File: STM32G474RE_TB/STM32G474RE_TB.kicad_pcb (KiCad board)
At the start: 2 copper layers, 4 parts, among them U1 STM32G474RETx, Y1 ABM8G-24.000MHZ-18-D2Y-T

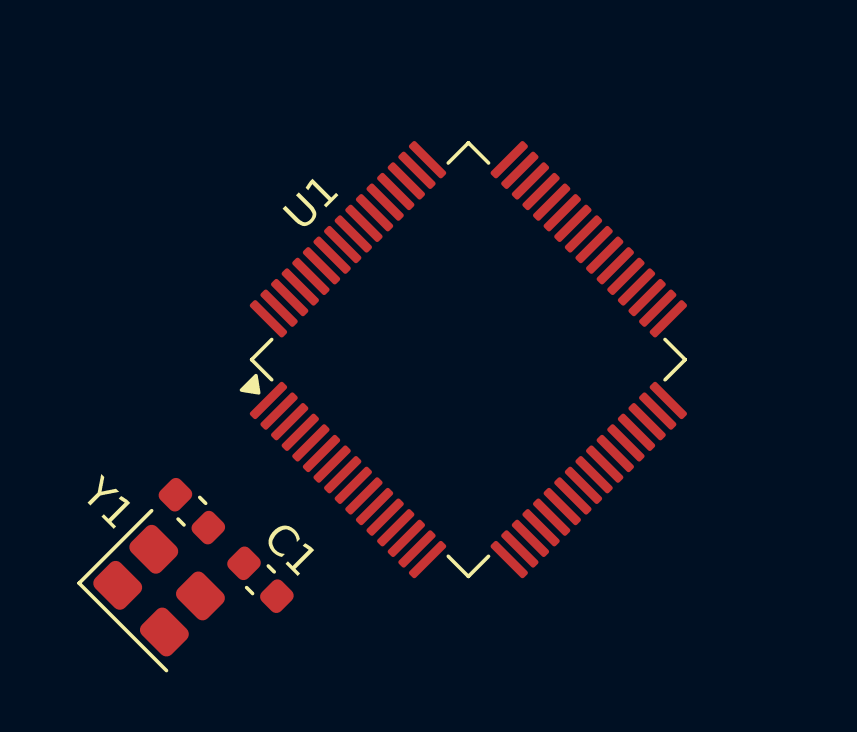
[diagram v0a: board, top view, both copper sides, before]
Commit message: Rotated STM32 and adjusted xosc capacitor values.
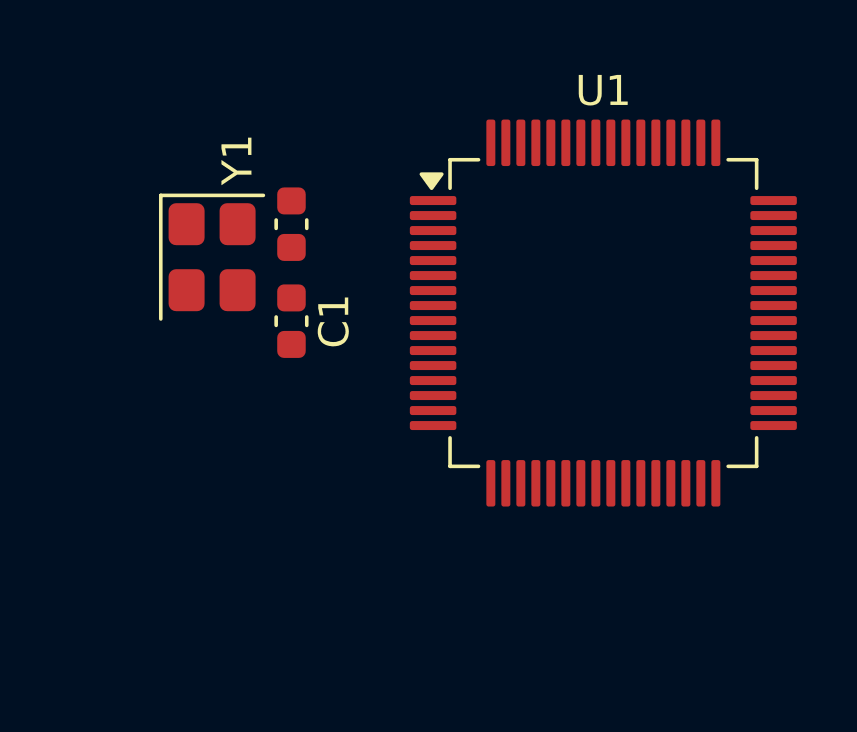
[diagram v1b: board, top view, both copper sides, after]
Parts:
- moved Y1 11.3 mm to (72.6, 35.7), turned to -90 degrees
- moved C2 10.1 mm to (75.2, 34.6), turned to 90 degrees
- moved C1 8.68 mm to (75.2, 37.9), turned to -90 degrees
- moved U1 4.76 mm to (85.6, 37.6), turned to 0 degrees

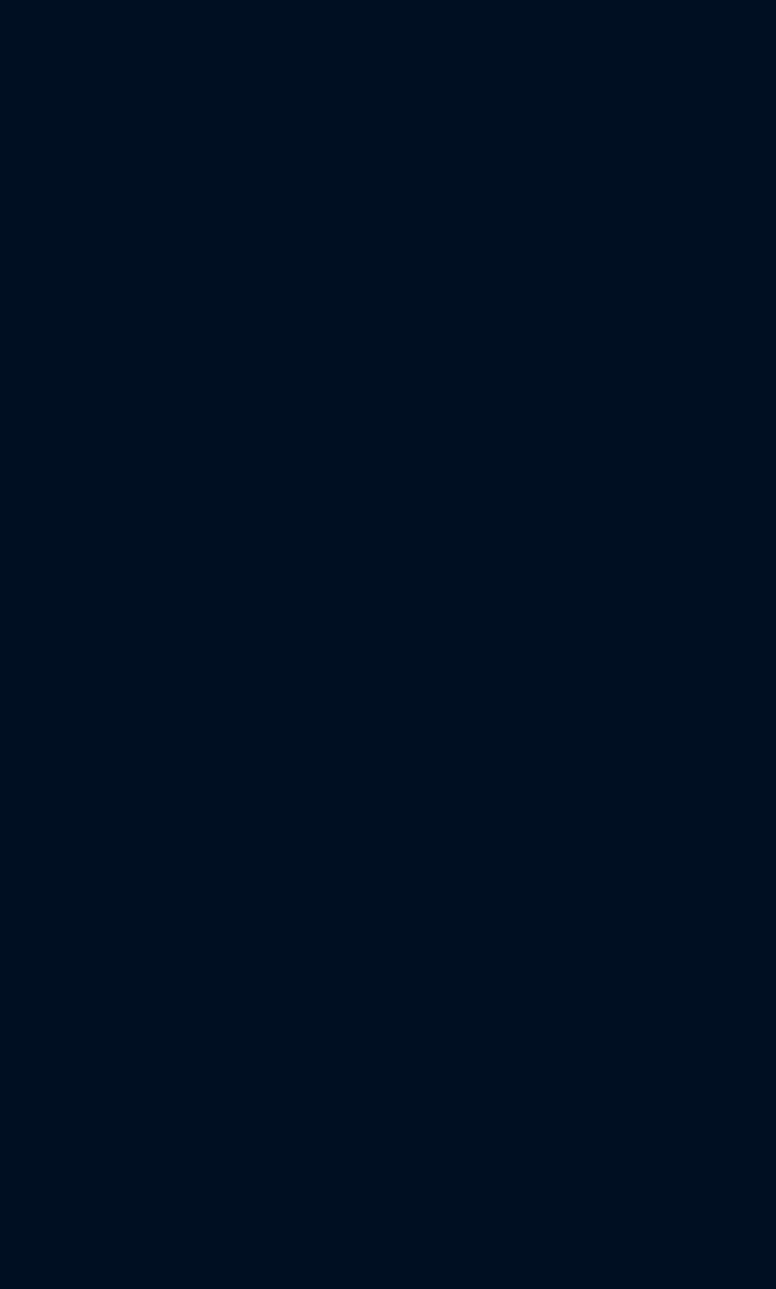
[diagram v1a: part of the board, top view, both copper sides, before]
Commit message: Added temporary STM32Cubeide project for pin config.
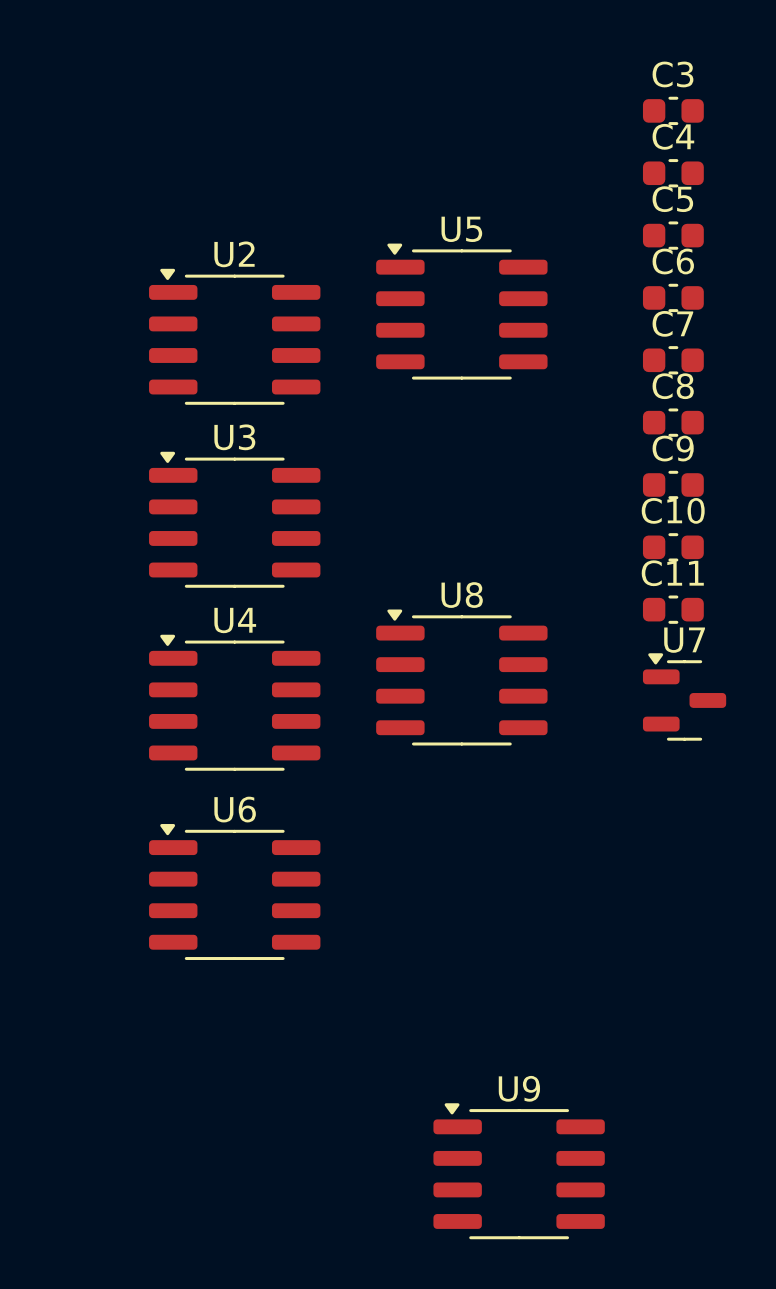
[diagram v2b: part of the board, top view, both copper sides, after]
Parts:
- added C10: 0.1uf, Capacitor_SMD:C_0603_1608Metric, F.Cu at (120.8, 39.9)
- added C11: 0.1uf, Capacitor_SMD:C_0603_1608Metric, F.Cu at (120.8, 42.4)
- added C3: 0.1uf, Capacitor_SMD:C_0603_1608Metric, F.Cu at (120.8, 22.3)
- added C4: 0.1uf, Capacitor_SMD:C_0603_1608Metric, F.Cu at (120.8, 24.8)
- added C5: 0.1uf, Capacitor_SMD:C_0603_1608Metric, F.Cu at (120.8, 27.3)
- added C6: 0.1uf, Capacitor_SMD:C_0603_1608Metric, F.Cu at (120.8, 29.8)
- added C7: 0.47uF, Capacitor_SMD:C_0603_1608Metric, F.Cu at (120.8, 32.3)
- added C8: 0.1uf, Capacitor_SMD:C_0603_1608Metric, F.Cu at (120.8, 34.8)
- added C9: 0.1uf, Capacitor_SMD:C_0603_1608Metric, F.Cu at (120.8, 37.3)
- added U2: MCP4921-ESN, Package_SO:SOIC-8_3.9x4.9mm_P1.27mm, F.Cu at (103.1, 31.5)
- added U3: MCP4921-ESN, Package_SO:SOIC-8_3.9x4.9mm_P1.27mm, F.Cu at (103.1, 38.9)
- added U4: MCP4921-ESN, Package_SO:SOIC-8_3.9x4.9mm_P1.27mm, F.Cu at (103.1, 46.2)
- added U5: OPA1678, Package_SO:SOIC-8_3.9x4.9mm_P1.27mm, F.Cu at (112.3, 30.5)
- added U6: MCP4921-ESN, Package_SO:SOIC-8_3.9x4.9mm_P1.27mm, F.Cu at (103.1, 53.8)
- added U7: REF3125, Package_TO_SOT_SMD:SOT-23, F.Cu at (121.2, 46.0)
- added U8: OPA1678, Package_SO:SOIC-8_3.9x4.9mm_P1.27mm, F.Cu at (112.3, 45.2)
- added U9: OPA1678, Package_SO:SOIC-8_3.9x4.9mm_P1.27mm, F.Cu at (114.6, 65.1)
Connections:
- U1 pad 35: unconnected-(U1-PB13-Pad35) -> /SPI1_SCK
- U1 pad 37: unconnected-(U1-PB15-Pad37) -> /SPI1_MOSI
- U1 pad 38: unconnected-(U1-PC6-Pad38) -> /DAC1_CS
- U1 pad 39: unconnected-(U1-PC7-Pad39) -> /DAC2_CS
- U1 pad 40: unconnected-(U1-PC8-Pad40) -> /DAC3_CS
- U1 pad 41: unconnected-(U1-PC9-Pad41) -> /DAC4_CS

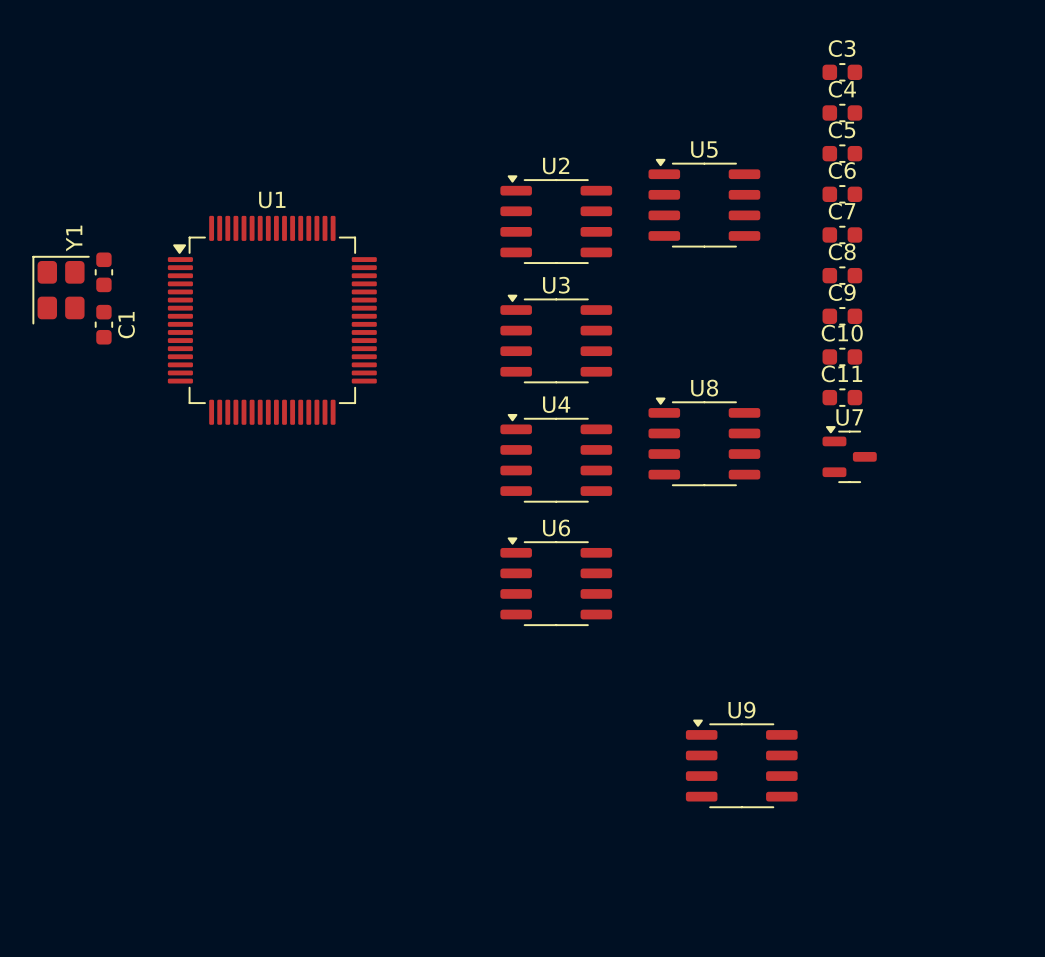
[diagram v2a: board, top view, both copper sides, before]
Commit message: Added power LDO and built DAC buffer circuits Added pin descriptions
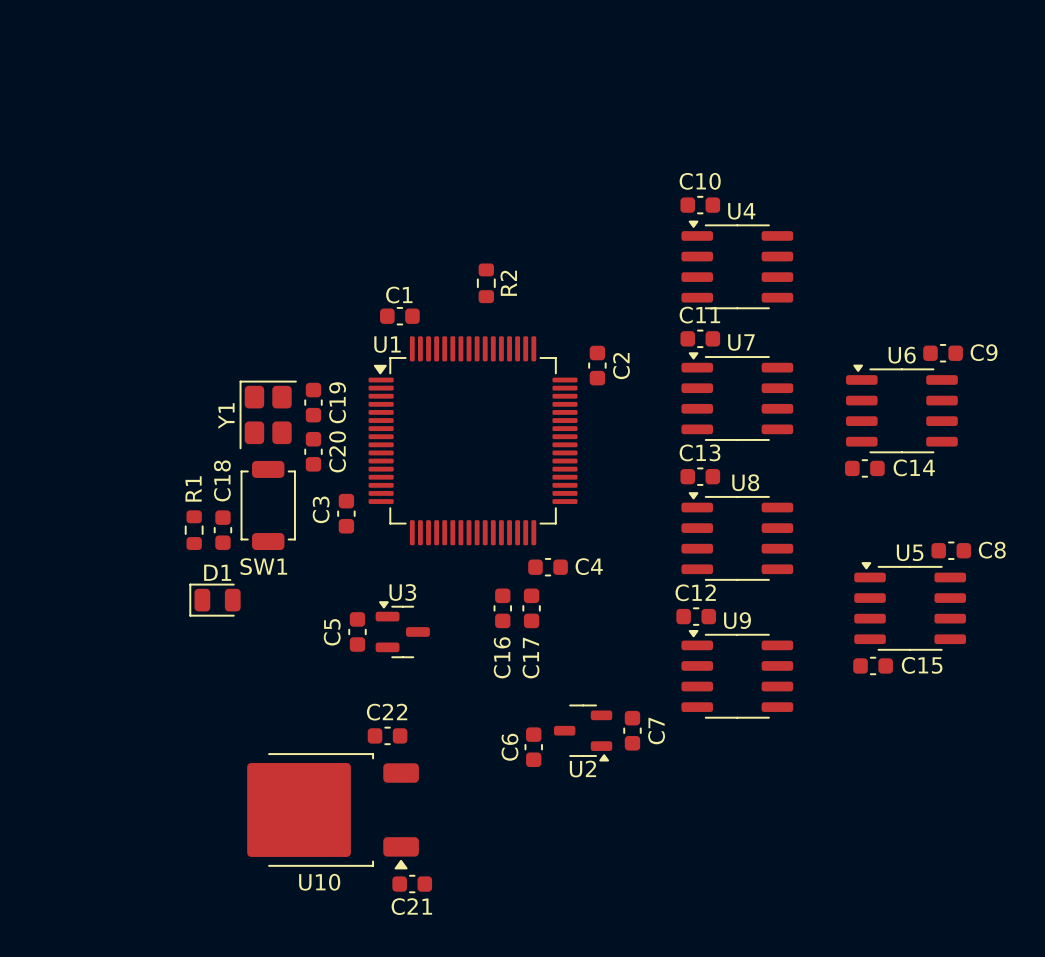
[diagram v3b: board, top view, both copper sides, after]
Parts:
- added C12: 0.1uf, Capacitor_SMD:C_0603_1608Metric, F.Cu at (111.8, 55.9)
- added C13: 0.1uf, Capacitor_SMD:C_0603_1608Metric, F.Cu at (112.0, 47.2)
- added C14: 0.1uf, Capacitor_SMD:C_0603_1608Metric, F.Cu at (122.2, 46.7)
- added C15: 0.1uf, Capacitor_SMD:C_0603_1608Metric, F.Cu at (122.7, 58.9)
- added C16: 0.1uf, Capacitor_SMD:C_0603_1608Metric, F.Cu at (99.8, 55.4)
- added C17: 1uf, Capacitor_SMD:C_0603_1608Metric, F.Cu at (101.6, 55.4)
- added C18: 0.1uf, Capacitor_SMD:C_0603_1608Metric, F.Cu at (82.5, 50.5)
- added C19: 22pf, Capacitor_SMD:C_0603_1608Metric, F.Cu at (88.1, 42.7)
- added C20: 22pf, Capacitor_SMD:C_0603_1608Metric, F.Cu at (88.1, 45.7)
- added C21: 0.33uf, Capacitor_SMD:C_0603_1608Metric, F.Cu at (94.2, 72.4)
- added C22: 0.1uf, Capacitor_SMD:C_0603_1608Metric, F.Cu at (92.7, 63.2)
- added D1: KT-0805G, LED_SMD:LED_0805_2012Metric, F.Cu at (82.2, 54.9)
- added R1: 10k, Resistor_SMD:R_0603_1608Metric, F.Cu at (80.8, 50.5)
- added R2: 100k, Resistor_SMD:R_0603_1608Metric, F.Cu at (98.8, 35.3)
- added SW1: TS-1088-AR02016, Button_Switch_SMD:SW_SPST_TS-1088-xR025, F.Cu at (85.3, 49.0)
- added U10: L7805, Package_TO_SOT_SMD:TO-252-2, F.Cu at (88.5, 67.8)
- C1, C2: value 22pf -> 100nF
- C3, C4: value 0.1uf -> 100nF
- C5: value 0.1uf -> 0.47uF
- C6: value 0.1uf -> 1u
- C7: value 0.47uF -> 1u
- U2: value MCP4921-ESN -> XC6206P332MR-G; footprint Package_SO:SOIC-8_3.9x4.9mm_P1.27mm -> Package_TO_SOT_SMD:SOT-23-3
- U3: value MCP4921-ESN -> REF3125; footprint Package_SO:SOIC-8_3.9x4.9mm_P1.27mm -> Package_TO_SOT_SMD:SOT-23
- U6: value MCP4921-ESN -> OPA1678
- U7: value REF3125 -> MCP4921-ESN; footprint Package_TO_SOT_SMD:SOT-23 -> Package_SO:SOIC-8_3.9x4.9mm_P1.27mm
- U8, U9: value OPA1678 -> MCP4921-ESN
- moved C5 42.0 mm to (90.9, 56.8), turned to -90 degrees
- moved C3 41.0 mm to (90.2, 49.5), turned to -90 degrees
- moved C6 39.1 mm to (101.7, 63.9), turned to 90 degrees
- moved C4 33.4 mm to (102.6, 52.8)
- moved C7 33.2 mm to (107.8, 62.9), turned to 90 degrees
- moved U2 31.5 mm to (104.8, 62.9), turned to 180 degrees
- moved C2 31.0 mm to (105.7, 40.4)
- moved U5 27.9 mm to (125.0, 55.4)
- moved U6 23.9 mm to (124.5, 43.2)
- moved U3 20.3 mm to (93.6, 56.8)
- moved C1 18.3 mm to (93.5, 37.3), turned to 180 degrees
- moved C8 18.3 mm to (127.5, 51.8)
- moved U4 16.4 mm to (114.3, 34.3)
- moved Y1 14.9 mm to (85.3, 43.4)
- moved U1 14.5 mm to (98.0, 45.0)
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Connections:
- C1 pad 1: Net-(U1-PF1) -> GND
- C1 pad 2: GND -> +3.3V
- C2 pad 1: Net-(U1-PF0) -> GND
- C2 pad 2: GND -> +3.3V
- C3 pad 1: -12V -> GND
- C3 pad 2: GND -> +3.3V
- C4 pad 1: +12V -> GND
- C4 pad 2: GND -> +3.3V
- C5 pad 1: +12V -> +3.3V
- C6 pad 1: -12V -> GND
- C6 pad 2: GND -> +5V
- C7 pad 1: +5V -> GND
- C7 pad 2: GND -> +3.3V
- C8 pad 1: +5V -> +12V
- C9 pad 1: +5V -> +12V
- U1 pad 1: unconnected-(U1-VBAT-Pad1) -> +3.3V
- U1 pad 15: Net-(U1-VSS-Pad15) -> GND
- U1 pad 16: unconnected-(U1-VDD-Pad16) -> +3.3V
- U1 pad 27: unconnected-(U1-VSSA-Pad27) -> GND
- U1 pad 28: unconnected-(U1-VREF+-Pad28) -> +2V5REF
- U1 pad 29: unconnected-(U1-VDDA-Pad29) -> +3.3V
- U1 pad 31: Net-(U1-VSS-Pad15) -> GND
- U1 pad 32: unconnected-(U1-VDD-Pad32) -> +3.3V
- U1 pad 47: Net-(U1-VSS-Pad15) -> GND
- U1 pad 48: unconnected-(U1-VDD-Pad48) -> +3.3V
- U1 pad 5: Net-(U1-PF0) -> /MCU_CONFIG/XOSC1
- U1 pad 55: unconnected-(U1-PD2-Pad55) -> /MCU_CONFIG/PD2/BOOT0
- U1 pad 6: Net-(U1-PF1) -> /MCU_CONFIG/XOSC2
- U1 pad 63: Net-(U1-VSS-Pad15) -> GND
- U1 pad 64: unconnected-(U1-VDD-Pad64) -> +3.3V
- U1 pad 7: unconnected-(U1-PG10-Pad7) -> /MCU_CONFIG/NRST
- U2 pad 1: +5V -> GND
- U2 pad 2: /DAC1_CS -> +3.3V
- U2 pad 3: /SPI1_MOSI -> +5V
- U3 pad 1: +5V -> +3.3V
- U3 pad 2: /DAC2_CS -> +2V5REF
- U3 pad 3: /SPI1_MOSI -> GND
- U4 pad 2: /DAC3_CS -> /DAC1_CS
- U4 pad 8: Net-(U4-VoutA) -> /SPI1_DACs/DAC1_out_nobuf
- U5 pad 1: /SPI1_DACs/DAC3_OUT -> /SPI1_DACs/DAC1_OUT
- U5 pad 2: /SPI1_DACs/DAC3_OUT -> /SPI1_DACs/DAC1_OUT
- U5 pad 3: Net-(U4-VoutA) -> /SPI1_DACs/DAC1_out_nobuf
- U5 pad 5: Net-(U5B-+) -> /SPI1_DACs/DAC2_out_nobuf
- U5 pad 6: /SPI1_DACs/DAC4_OUT -> /SPI1_DACs/DAC2_OUT
- U5 pad 7: /SPI1_DACs/DAC4_OUT -> /SPI1_DACs/DAC2_OUT
- U6 pad 1: +5V -> /SPI1_DACs/DAC3_OUT
- U6 pad 2: /DAC4_CS -> /SPI1_DACs/DAC3_OUT
- U6 pad 3: /SPI1_MOSI -> /SPI1_DACs/DAC3_out_nobuf
- U6 pad 4: /SPI1_SCK -> -12V
- U6 pad 5: GND -> /SPI1_DACs/DAC4_out_nobuf
- U6 pad 6: +2V5REF -> /SPI1_DACs/DAC4_OUT
- U6 pad 7: GND -> /SPI1_DACs/DAC4_OUT
- U6 pad 8: Net-(U5B-+) -> +12V
- U7 pad 2: +2V5REF -> /DAC2_CS
- U7 pad 3: GND -> /SPI1_MOSI
- U8 pad 1: /SPI1_DACs/DAC3_OUT -> +5V
- U8 pad 2: /SPI1_DACs/DAC3_OUT -> /DAC3_CS
- U8 pad 3: Net-(U4-VoutA) -> /SPI1_MOSI
- U8 pad 4: -12V -> /SPI1_SCK
- U8 pad 5: Net-(U6-VoutA) -> GND
- U8 pad 6: /SPI1_DACs/DAC4_OUT -> +2V5REF
- U8 pad 7: /SPI1_DACs/DAC4_OUT -> GND
- U8 pad 8: +12V -> /SPI1_DACs/DAC3_out_nobuf
- U9 pad 1: /SPI1_DACs/DAC1_OUT -> +5V
- U9 pad 2: /SPI1_DACs/DAC1_OUT -> /DAC4_CS
- U9 pad 3: Net-(U2-VoutA) -> /SPI1_MOSI
- U9 pad 4: -12V -> /SPI1_SCK
- U9 pad 5: Net-(U3-VoutA) -> GND
- U9 pad 6: /SPI1_DACs/DAC2_OUT -> +2V5REF
- U9 pad 7: /SPI1_DACs/DAC2_OUT -> GND
- U9 pad 8: +12V -> /SPI1_DACs/DAC4_out_nobuf
- Y1 pad 1: Net-(U1-PF0) -> /MCU_CONFIG/XOSC1
- Y1 pad 3: Net-(U1-PF1) -> /MCU_CONFIG/XOSC2
